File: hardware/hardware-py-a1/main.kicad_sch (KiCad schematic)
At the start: 64 parts, among them J6 USB_C_Receptacle_USB2.0_16P, J7 Conn_02x08_Odd_Even, Q6 BSS138, SW1 SW_Push, SW10 SW_Push, SW11 SW_Push, SW12 SW_Push, SW13 SW_Push, SW14 SW_Push, SW15 SW_Push, SW16 SW_Push, SW17 SW_Push, SW18 SW_Push, SW19 SW_Push, SW2 SW_Push, SW20 SW_Push, SW21 Encoder, SW22 SW_Push, SW3 SW_Push, SW4 SW_Push, SW5 SW_Push, SW6 SW_Push, SW7 SW_Push, SW8 SW_Push, SW9 SW_Push, U3 74HC595, U4 ESP32-S3-WROOM-1

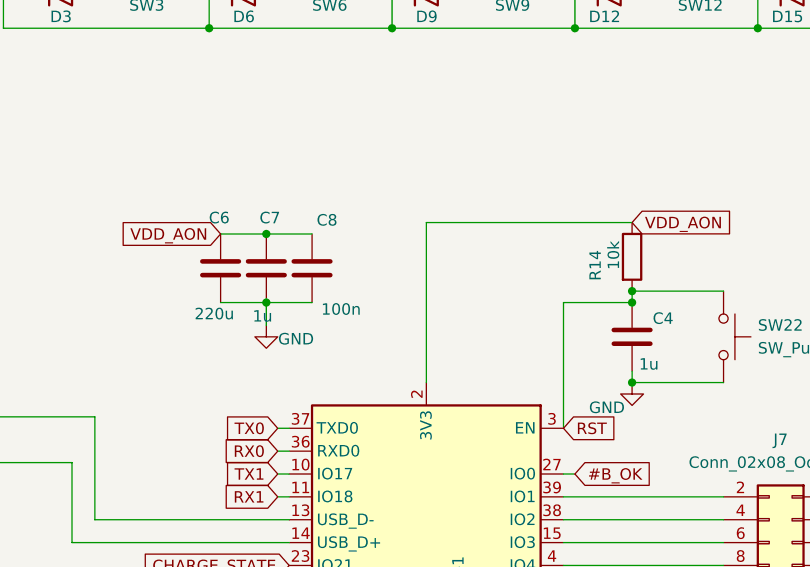
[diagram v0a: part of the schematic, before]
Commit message: hw: passives values simpler, tantlum caps, silkscreen tweaks
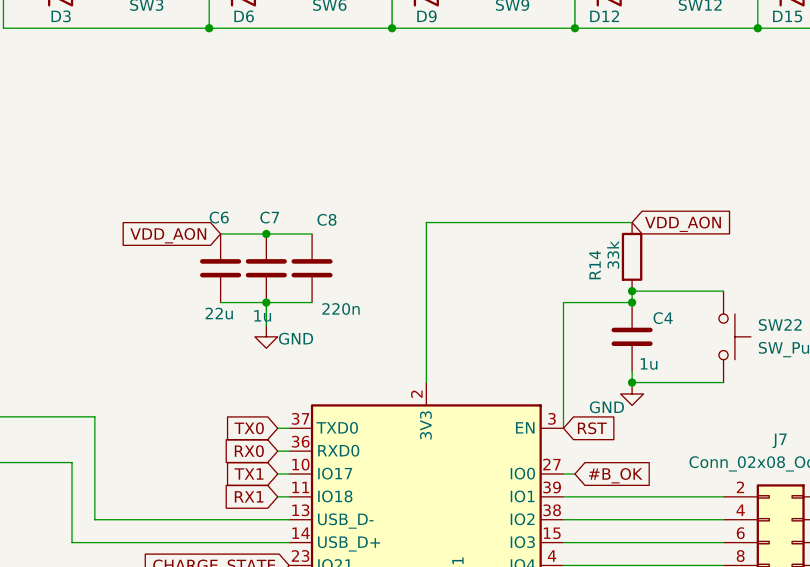
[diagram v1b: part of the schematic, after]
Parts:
- C20, C21, C4: footprint Capacitor_SMD:C_0805_2012Metric -> Capacitor_SMD:C_0805_2012Metric_Pad1.18x1.45mm_HandSolder
- C6: value 220u -> 22u; footprint Capacitor_SMD:C_2220_5750Metric -> Capacitor_SMD:C_1206_3216Metric_Pad1.33x1.80mm_HandSolder
- C7: footprint Capacitor_SMD:C_1206_3216Metric -> Capacitor_SMD:C_0805_2012Metric_Pad1.18x1.45mm_HandSolder
- C8: value 100n -> 220n; footprint Capacitor_SMD:C_0805_2012Metric -> Capacitor_SMD:C_0805_2012Metric_Pad1.18x1.45mm_HandSolder
- D1, D10, D11, D12, D13, D14, D15, D16, D17, D18, D19, D2, D20, D3, D4, D45, D46, D5, D6, D7, D8, D9: value D -> 1N4148
- R14: value 10k -> 33k
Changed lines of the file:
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@@
 			)
 		)
-		(property "Value" "D"
+		(property "Value" "1N4148"
 			(at 123.19 53.34 90)
 			(effects
@@
 			)
 		)
-		(property "Value" "D"
+		(property "Value" "1N4148"
 			(at 123.19 63.5 90)
 			(effects
@@
 			)
 		)
-		(property "Value" "100n"
+		(property "Value" "220n"
 			(at 112.776 106.172 0)
 			(effects
@@
 			)
 		)
-		(property "Footprint" "Capacitor_SMD:C_0805_2012Metric"
+		(property "Footprint" "Capacitor_SMD:C_0805_2012Metric_Pad1.18x1.45mm_HandSolder"
 			(at 112.7252 105.41 0)
 			(effects
@@
 			)
 		)
-		(property "Value" "D"
+		(property "Value" "1N4148"
 			(at 143.51 63.5 90)
 			(effects
@@
 			)
 		)
-		(property "Value" "D"
+		(property "Value" "1N4148"
 			(at 102.87 53.34 90)
 			(effects
@@
 			)
 		)
-		(property "Value" "D"
+		(property "Value" "1N4148"
 			(at 163.83 53.34 90)
 			(effects
@@
 			)
 		)
-		(property "Footprint" "Capacitor_SMD:C_0805_2012Metric"
+		(property "Footprint" "Capacitor_SMD:C_0805_2012Metric_Pad1.18x1.45mm_HandSolder"
 			(at 82.2452 167.64 0)
 			(effects
@@
 			)
 		)
-		(property "Value" "D"
+		(property "Value" "1N4148"
 			(at 204.47 63.5 90)
 			(effects
@@
 			)
 		)
-		(property "Value" "D"
+		(property "Value" "1N4148"
 			(at 163.83 63.5 90)
 			(effects
@@
 			)
 		)
-		(property "Value" "D"
+		(property "Value" "1N4148"
 			(at 223.52 57.15 90)
 			(effects
@@
 			)
 		)
-		(property "Footprint" "Capacitor_SMD:C_1206_3216Metric"
+		(property "Footprint" "Capacitor_SMD:C_0805_2012Metric_Pad1.18x1.45mm_HandSolder"
 			(at 107.6452 105.41 0)
 			(effects
@@
 			)
 		)
-		(property "Value" "D"
+		(property "Value" "1N4148"
 			(at 163.83 73.66 90)
 			(effects
@@
 			)
 		)
-		(property "Value" "D"
+		(property "Value" "1N4148"
 			(at 102.87 63.5 90)
 			(effects
@@
 			)
 		)
-		(property "Value" "D"
+		(property "Value" "1N4148"
 			(at 82.55 63.5 90)
 			(effects
@@
 			)
 		)
-		(property "Value" "D"
+		(property "Value" "1N4148"
 			(at 184.15 53.34 90)
 			(effects
@@
 			)
 		)
-		(property "Value" "D"
+		(property "Value" "1N4148"
 			(at 184.15 73.66 90)
 			(effects
@@
 			)
 		)
-		(property "Value" "D"
+		(property "Value" "1N4148"
 			(at 82.55 73.66 90)
 			(effects
@@
 			)
 		)
-		(property "Value" "D"
+		(property "Value" "1N4148"
 			(at 223.52 67.31 90)
 			(effects
@@
 			)
 		)
-		(property "Value" "D"
+		(property "Value" "1N4148"
 			(at 123.19 73.66 90)
 			(effects
@@
 			)
 		)
-		(property "Value" "D"
+		(property "Value" "1N4148"
 			(at 102.87 73.66 90)
 			(effects
@@
 			)
 		)
-		(property "Value" "D"
+		(property "Value" "1N4148"
 			(at 143.51 53.34 90)
 			(effects
@@
 			)
 		)
-		(property "Footprint" "Capacitor_SMD:C_0805_2012Metric"
+		(property "Footprint" "Capacitor_SMD:C_0805_2012Metric_Pad1.18x1.45mm_HandSolder"
 			(at 148.2852 113.03 0)
 			(effects
@@
 			)
 		)
-		(property "Value" "D"
+		(property "Value" "1N4148"
 			(at 184.15 63.5 90)
 			(effects
@@
 			)
 		)
-		(property "Value" "220u"
+		(property "Value" "22u"
 			(at 103.124 106.68 0)
 			(effects
@@
 			)
 		)
-		(property "Footprint" "Capacitor_SMD:C_2220_5750Metric"
+		(property "Footprint" "Capacitor_SMD:C_1206_3216Metric_Pad1.33x1.80mm_HandSolder"
 			(at 100.6348 105.41 0)
 			(effects
@@
 			)
 		)
-		(property "Value" "D"
+		(property "Value" "1N4148"
 			(at 82.55 53.34 90)
 			(effects
@@
 			)
 		)
-		(property "Value" "D"
+		(property "Value" "1N4148"
 			(at 143.51 73.66 90)
 			(effects
@@
 			)
 		)
-		(property "Value" "10k"
+		(property "Value" "33k"
 			(at 145.288 98.552 90)
 			(effects
@@
 			)
 		)
-		(property "Value" "D"
+		(property "Value" "1N4148"
 			(at 204.47 53.34 90)
 			(effects
@@
 			)
 		)
-		(property "Footprint" "Capacitor_SMD:C_0805_2012Metric"
+		(property "Footprint" "Capacitor_SMD:C_0805_2012Metric_Pad1.18x1.45mm_HandSolder"
 			(at 89.8652 167.64 0)
 			(effects
